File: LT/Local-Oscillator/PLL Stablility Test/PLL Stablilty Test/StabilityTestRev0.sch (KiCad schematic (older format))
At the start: 71 parts, among them J1 Conn_01x02_Male, J10 Conn_Coaxial, J11 Conn_Coaxial, J13 Conn_01x02_Male, J17 Conn_01x02_Male, J18 Conn_Coaxial, J20 Conn_01x02_Male, J3 Conn_Coaxial, J4 Conn_01x04_Male, J6 Conn_01x02_Male, J7 Conn_01x02_Male, J8 Conn_01x02_Male, J9 Conn_01x03_Male, Q1 2N5486 JFET, Q2 2N5486 JFET, U1 LMX231X, U2 L7808, U3 LMH6611, U4 LMH6611

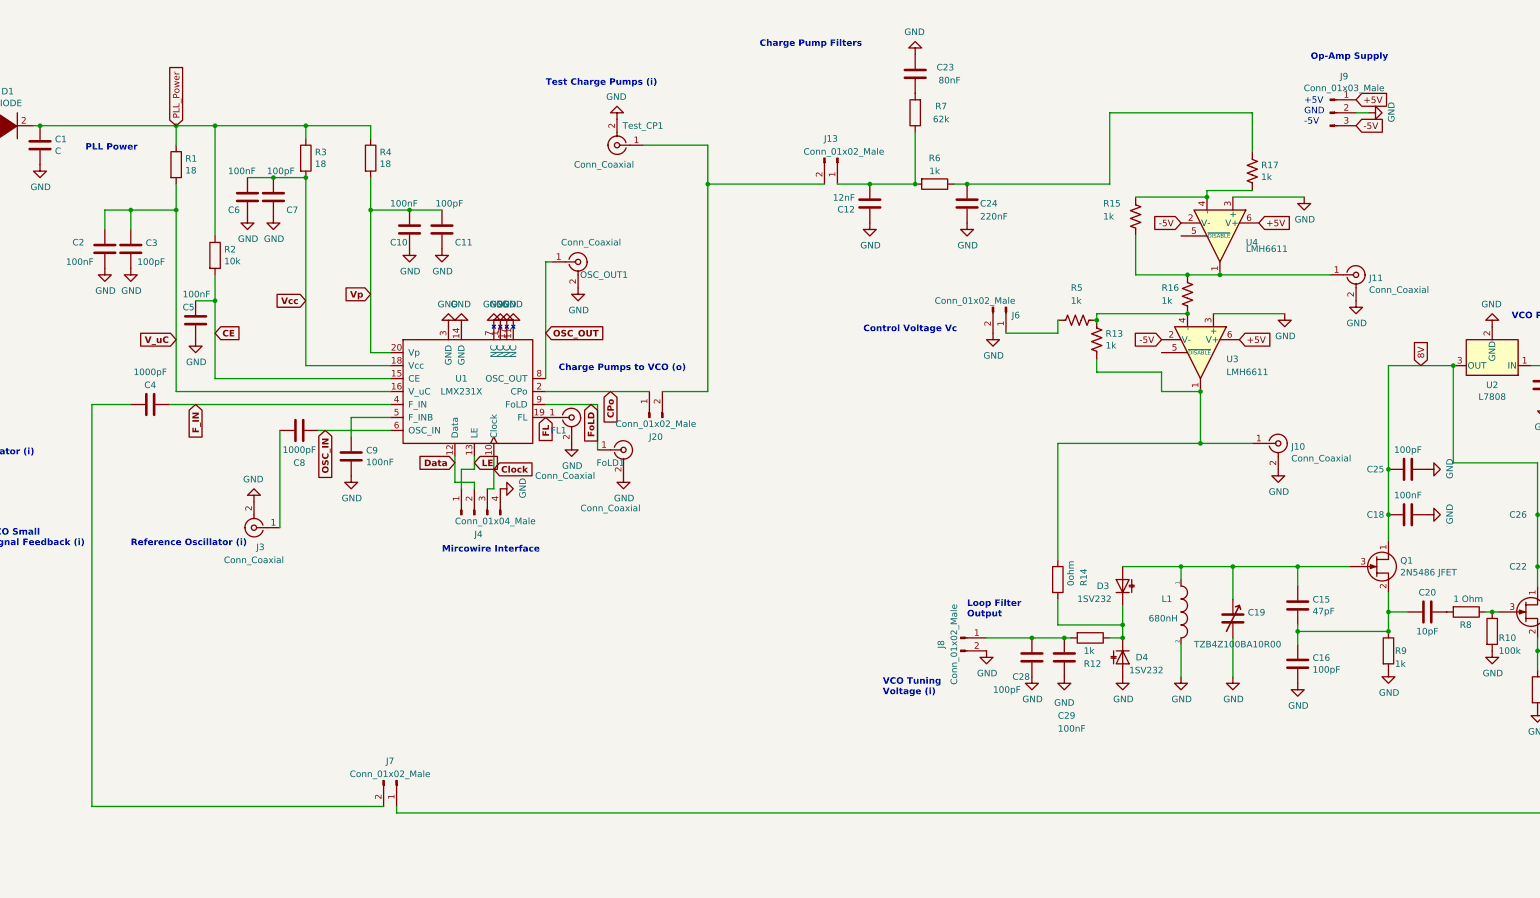
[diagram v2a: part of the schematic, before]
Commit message: deleted some unnecassary headers in the PLL stability test board
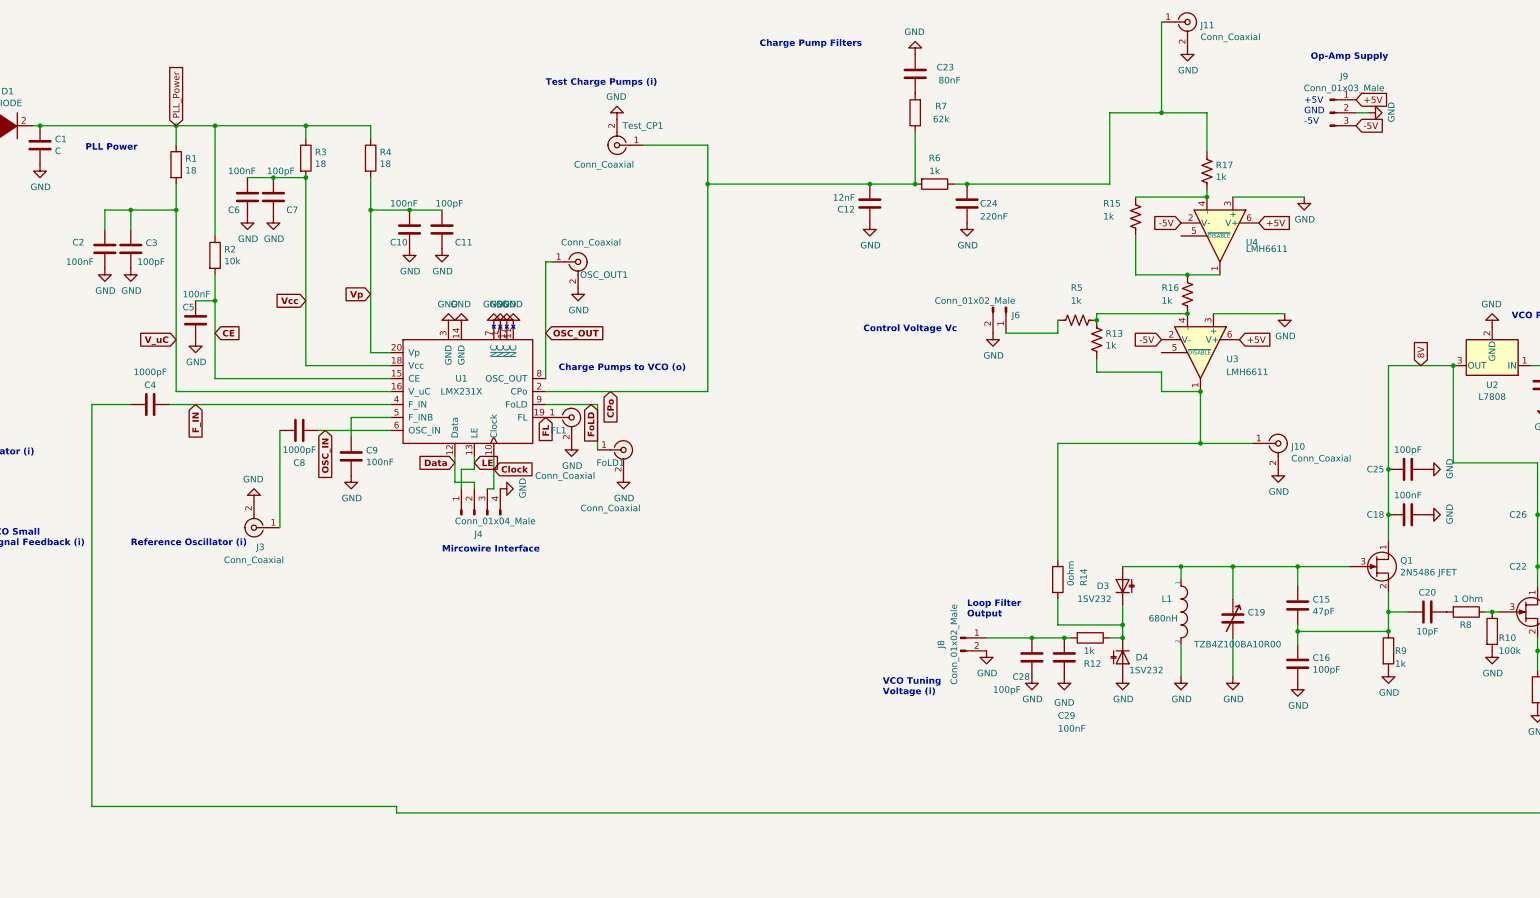
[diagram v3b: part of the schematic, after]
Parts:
- removed J13, J20, J7: Conn_01x02_Male, Connector_PinHeader_2.54mm:PinHeader_1x02_P2.54mm_Vertical, symbol Connector:Conn_01x02_Male
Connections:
- net CPo: now also C12.2, R6.2, R7.1, Test_CP1.1 (In)
- net at C4.1: now also C17.1, Q2.2 (S), R11.1
- net at C24.1, R17.1, R6.1: now also J11.1 (In)
- net at R15.1, R16.1, U4.1: no longer J11.1 (In)
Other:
- moved on the sheet: J11, R17
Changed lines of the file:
@@
 Wire Wire Line
 	6600 4550 6600 4900
-$Comp
-L Connector:Conn_01x02_Male J7
-U 1 1 5C868E39
-P 5050 7450
-F 0 "J7" V 4900 7400 50  0000 C CNN
-F 1 "Conn_01x02_Male" V 5000 7400 50  0000 C CNN
-F 2 "Connector_PinHeader_2.54mm:PinHeader_1x02_P2.54mm_Vertical" H 5050 7450 50  0001 C CNN
-F 3 "~" H 5050 7450 50  0001 C CNN
-	1    5050 7450
-	0    1    1    0
-$EndComp
 Wire Wire Line
 	5050 7700 5050 7650
-Wire Wire Line
-	4950 7650 2700 7650
 $Comp
 L Connector:Conn_Coaxial FL1
@@
 Text Notes 6200 2100 0    50   ~ 10
 Test Charge Pumps (i)
-$Comp
-L Connector:Conn_01x02_Male J20
-U 1 1 5C7EAF41
-P 7000 4650
-F 0 "J20" V 6850 4600 50  0000 C CNN
-F 1 "Conn_01x02_Male" V 6950 4600 50  0000 C CNN
-F 2 "Connector_PinHeader_2.54mm:PinHeader_1x02_P2.54mm_Vertical" H 7000 4650 50  0001 C CNN
-F 3 "~" H 7000 4650 50  0001 C CNN
-	1    7000 4650
-	0    -1   -1   0
-$EndComp
-Wire Wire Line
-	6200 4450 7000 4450
-Wire Wire Line
-	7100 4450 7450 4450
 Wire Wire Line
 	5650 4950 5650 5050
@@
 	10750 3250 10750 3550
 Wire Wire Line
-	11650 2600 11650 2300
-Wire Wire Line
-	11300 2900 11650 2900
+	11300 2600 11300 2300
 Wire Wire Line
 	11300 2950 11300 2900
@@
 L Device:R_US R17
 U 1 1 5E5AD2CA
-P 11650 2750
-F 0 "R17" H 11718 2796 50  0000 L CNN
-F 1 "1k" H 11718 2705 50  0000 L CNN
-F 2 "Resistor_SMD:R_0805_2012Metric_Pad1.15x1.40mm_HandSolder" V 11690 2740 50  0001 C CNN
-F 3 "~" H 11650 2750 50  0001 C CNN
-	1    11650 2750
+P 11300 2750
+F 0 "R17" H 11368 2796 50  0000 L CNN
+F 1 "1k" H 11368 2705 50  0000 L CNN
+F 2 "Resistor_SMD:R_0805_2012Metric_Pad1.15x1.40mm_HandSolder" V 11340 2740 50  0001 C CNN
+F 3 "~" H 11300 2750 50  0001 C CNN
+	1    11300 2750
 	1    0    0    -1
 $EndComp
@@
 Wire Wire Line
 	8700 2850 9050 2850
-Wire Wire Line
-	8450 2850 8700 2850
 $Comp
 L Device:C C12
@@
 Text Notes 7850 1800 0    50   ~ 10
 Charge Pump Filters
-$Comp
-L Connector:Conn_01x02_Male J13
-U 1 1 5C886707
-P 8450 2650
-F 0 "J13" V 8300 2600 50  0000 C CNN
-F 1 "Conn_01x02_Male" V 8400 2700 50  0000 C CNN
-F 2 "Connector_PinHeader_2.54mm:PinHeader_1x02_P2.54mm_Vertical" H 8450 2650 50  0001 C CNN
-F 3 "~" H 8450 2650 50  0001 C CNN
-	1    8450 2650
-	0    1    1    0
-$EndComp
 $Comp
 L Device:C C15
@@
 L power:GND #PWR0109
 U 1 1 5E5C1BFD
-P 12450 3750
-F 0 "#PWR0109" H 12450 3500 50  0001 C CNN
-F 1 "GND" H 12455 3577 50  0000 C CNN
-F 2 "" H 12450 3750 50  0001 C CNN
-F 3 "" H 12450 3750 50  0001 C CNN
-	1    12450 3750
+P 11150 1800
+F 0 "#PWR0109" H 11150 1550 50  0001 C CNN
+F 1 "GND" H 11155 1627 50  0000 C CNN
+F 2 "" H 11150 1800 50  0001 C CNN
+F 3 "" H 11150 1800 50  0001 C CNN
+	1    11150 1800
 	1    0    0    -1
 $EndComp
@@
 Wire Wire Line
 	10150 5750 10150 4850
-Wire Wire Line
-	7450 2850 8350 2850
 Connection ~ 7450 2850
 Wire Wire Line
@@
 	10150 4850 11250 4850
 Wire Wire Line
-	10550 2300 11650 2300
+	10550 2300 10950 2300
 $Comp
 L Connector:Conn_Coaxial J11
 U 1 1 5E5B37F5
-P 12450 3550
-F 0 "J11" H 12550 3525 50  0000 L CNN
-F 1 "Conn_Coaxial" H 12550 3434 50  0000 L CNN
-F 2 "Connector_Coaxial:SMA_Amphenol_132289_EdgeMount" H 12450 3550 50  0001 C CNN
-F 3 " ~" H 12450 3550 50  0001 C CNN
-	1    12450 3550
-	1    0    0    -1
-$EndComp
-Wire Wire Line
-	11400 3550 12250 3550
-Connection ~ 11400 3550
+P 11150 1600
+F 0 "J11" H 11250 1575 50  0000 L CNN
+F 1 "Conn_Coaxial" H 11250 1484 50  0000 L CNN
+F 2 "Connector_Coaxial:SMA_Amphenol_132289_EdgeMount" H 11150 1600 50  0001 C CNN
+F 3 " ~" H 11150 1600 50  0001 C CNN
+	1    11150 1600
+	1    0    0    -1
+$EndComp
 $Comp
 L Connector:Conn_Coaxial J10
@@
 	1    0    0    -1
 $EndComp
+Wire Wire Line
+	6200 4450 7450 4450
+Wire Wire Line
+	7450 2850 8700 2850
+Wire Wire Line
+	2700 7650 5050 7650
+Wire Wire Line
+	10950 1600 10950 2300
+Connection ~ 10950 2300
+Wire Wire Line
+	10950 2300 11300 2300
 $EndSCHEMATC
